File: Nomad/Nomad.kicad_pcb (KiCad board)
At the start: 2 copper layers, 61 parts, among them J1 Barrel_Jack, J2 Conn_01x04_Socket, J3 Conn_01x04_Socket, J4 Conn_01x02_Socket, J5 Conn_01x02_Socket, U1 ESP32-DEVKITC-32UE, U2 BU18SD5WG-TL, U3 BU33SD5WG-TR, U4 XL1509-5.0, U5 PTAS2780RYAR

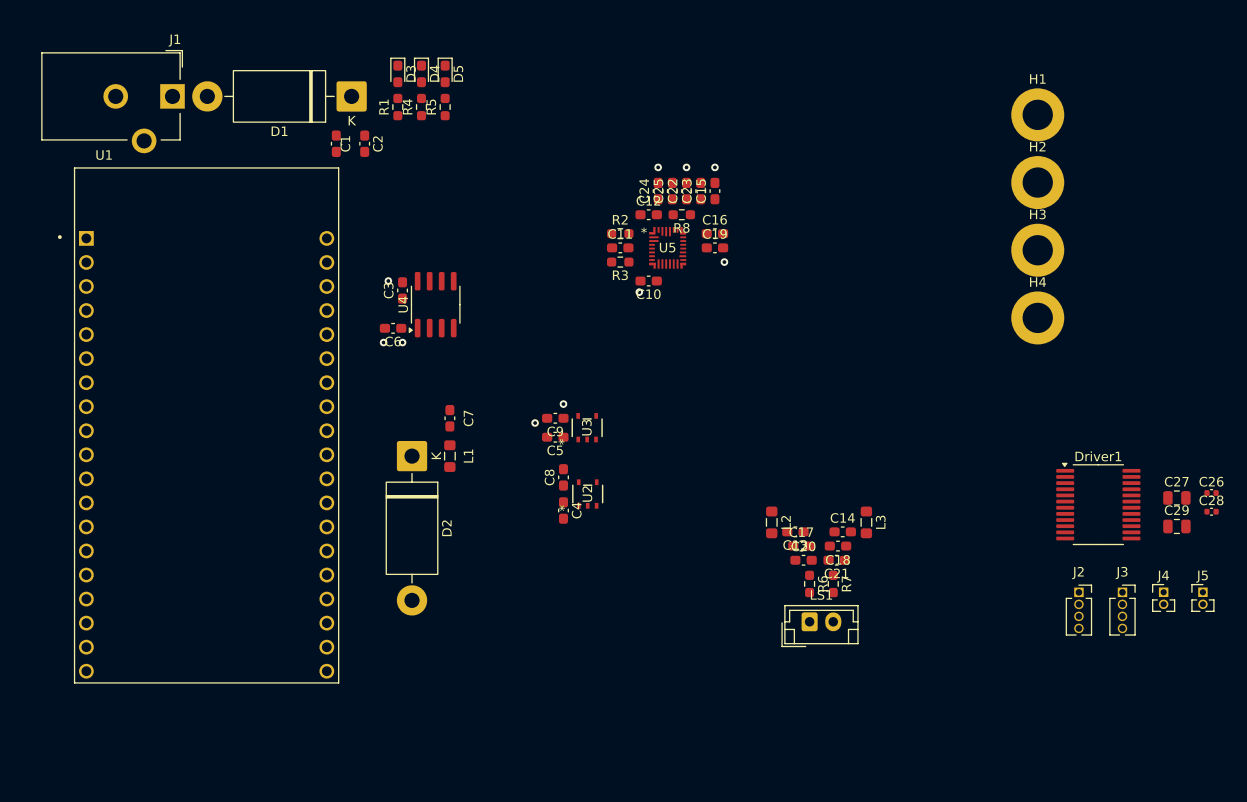
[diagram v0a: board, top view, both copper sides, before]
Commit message: routage pcb
finitions placement composants + routage
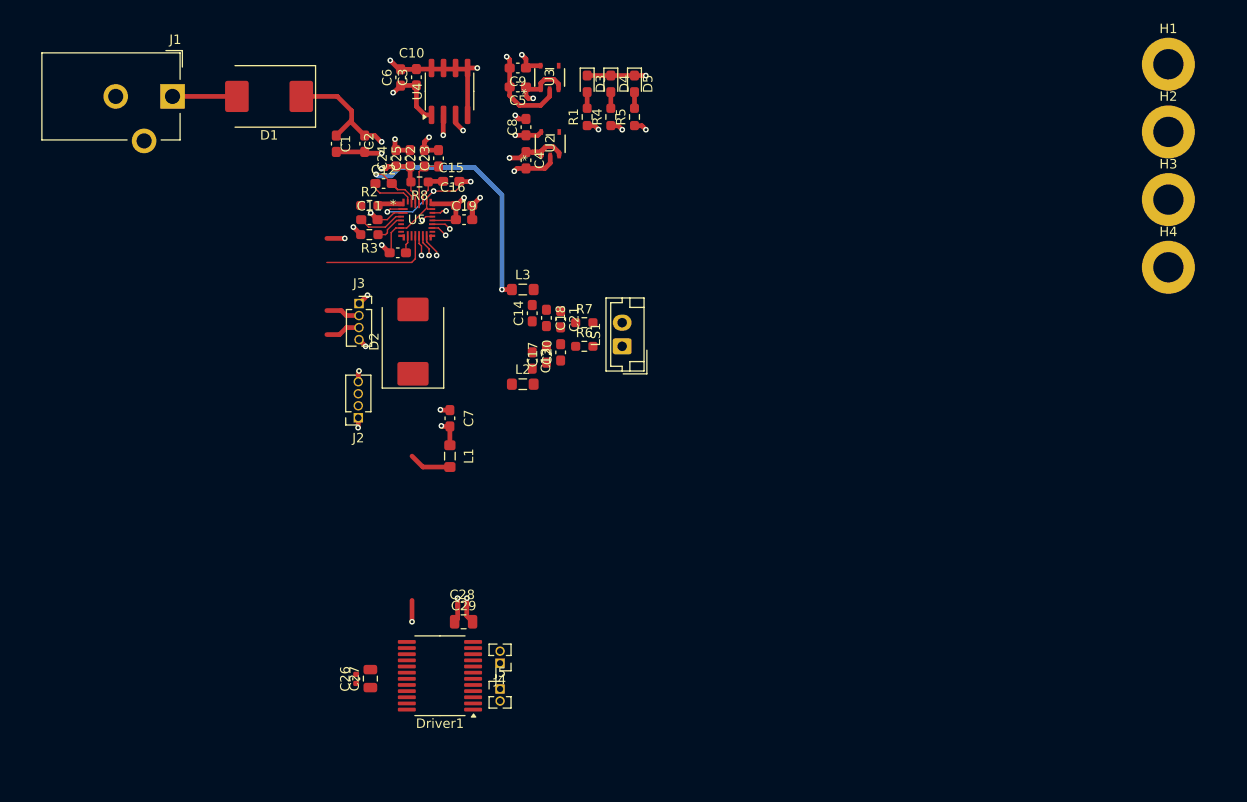
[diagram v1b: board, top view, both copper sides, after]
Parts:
- removed U1: ESP32-DEVKITC-32UE, footprints:ESPRESSIF_ESP32-DEVKITC-32UE
- D1, D2: value 1N5820 -> MBRS320; footprint Diode_THT:D_DO-201AD_P15.24mm_Horizontal -> Diode_SMD:D_SMC
- moved C26 92.5 mm to (108.1, 96.5), turned to 90 degrees
- moved C27 87.3 mm to (109.6, 96.5), turned to 90 degrees
- moved J3 86.2 mm to (108.4, 56.9)
- moved C28 79.8 mm to (119.3, 88.8)
- moved J2 78.3 mm to (108.3, 69.0), turned to 180 degrees
- moved C29 76.0 mm to (119.5, 90.5)
- moved J5 75.0 mm to (123.3, 97.6)
- moved Driver1 71.9 mm to (117.0, 96.2), turned to 180 degrees
- moved J4 70.5 mm to (123.3, 94.9), turned to 180 degrees
- moved L3 43.9 mm to (125.7, 55.4), turned to 0 degrees
- moved C14 40.1 mm to (126.7, 57.9), turned to 90 degrees
- moved C18 39.1 mm to (128.2, 58.4), turned to -90 degrees
- moved C21 38.7 mm to (129.7, 58.5), turned to -90 degrees
- moved R7 38.1 mm to (132.2, 58.9), turned to 0 degrees
- moved C4 37.2 mm to (126.0, 41.7)
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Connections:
- C26 pad 1: +3.3V -> 3.3V
- C27 pad 1: +3.3V -> 3.3V
- Driver1 pad 20: +3.3V -> 3.3V
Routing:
- net GND: track 0.00 -> 116.0 mm, vias 0 -> 20
- net 12V: track 0.00 -> 64.9 mm, vias 0 -> 5
- net /OUT_N: track 0.00 -> 32.4 mm, vias 0 -> 2
- net 5V: track 0.00 -> 31.4 mm, vias 0 -> 6
- net 1.8V: track 0.00 -> 26.7 mm, vias 0 -> 3
- net 3.3V: track 0.00 -> 18.5 mm, vias 0 -> 2
- net SDOUT: track 0.00 -> 11.9 mm
- net Net-(D1-A): track 0.00 -> 6.80 mm
- net Net-(D2-K): track 0.00 -> 6.64 mm, vias 0 -> 1
- net Net-(U5-VBAT1S): track 0.00 -> 5.64 mm
- net Net-(U5-BST_N): track 0.00 -> 5.56 mm
- net Net-(U5-BST_P): track 0.00 -> 4.99 mm
- net /OUT_P: track 0.00 -> 4.15 mm, vias 0 -> 1
- net Net-(U5-PVDD_SNS): track 0.00 -> 3.88 mm
- net Echo_cap_1: track 0.00 -> 3.71 mm
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- added copper zone on In2.Cu, net GND
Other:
- copper layers 2 -> 4

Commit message: Fin routage
Fin routage sauf pour esp
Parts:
- moved H1 96.6 mm to (109.1, 77.8)
- moved H2 86.2 mm to (107.9, 33.0)
- moved H4 63.2 mm to (136.0, 78.3)
- moved H3 62.8 mm to (135.4, 68.8)
- moved Driver1 48.7 mm to (131.0, 49.5)
- moved C28 48.7 mm to (133.3, 42.1)
- moved C29 48.7 mm to (133.5, 43.9)
- moved J4 48.7 mm to (137.3, 48.2)
- moved J5 48.7 mm to (137.3, 51.0)
- moved C26 48.7 mm to (122.2, 49.9)
- moved C27 48.7 mm to (123.7, 49.9)
- moved C7 35.6 mm to (122.1, 33.6)
- moved L1 35.6 mm to (122.1, 37.6)
- moved D2 6.90 mm to (119.5, 56.6), turned to -90 degrees
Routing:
- net GND: track 116.0 -> 142.6 mm, vias 20 -> 21
- net /OUT_P: track 4.15 -> 30.5 mm, vias 1 -> 2
- net 12V: track 64.9 -> 80.1 mm
- net Net-(D2-K): track 6.64 -> 21.7 mm, vias 1 -> 2
- net /VSNS_N: track 0.00 -> 12.9 mm
- net /VSNS_P: track 1.12 -> 13.9 mm
- net 3.3V: track 18.5 -> 25.0 mm, vias 2 -> 3
- net AO2: track 0.00 -> 3.68 mm
- net BO2: track 0.00 -> 3.65 mm
- net BO1: track 0.00 -> 3.63 mm
- net AO1: track 0.00 -> 3.61 mm
- net Net-(C20-Pad1): track 0.00 -> 2.21 mm
- net STBY: track 0.00 -> 2.16 mm, vias 0 -> 1
- net Net-(C21-Pad1): track 0.00 -> 2.09 mm

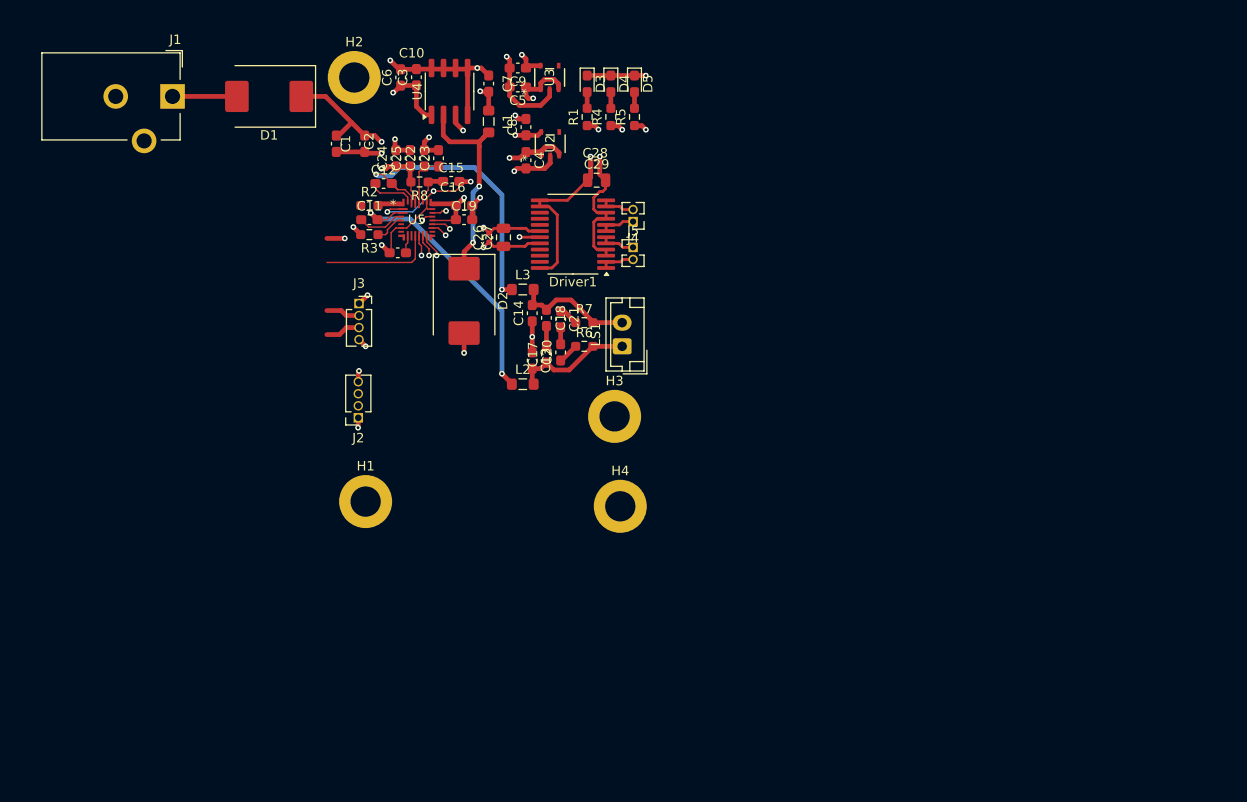
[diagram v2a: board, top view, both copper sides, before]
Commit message: Finished routing and silkscreen placement
todo Gerber
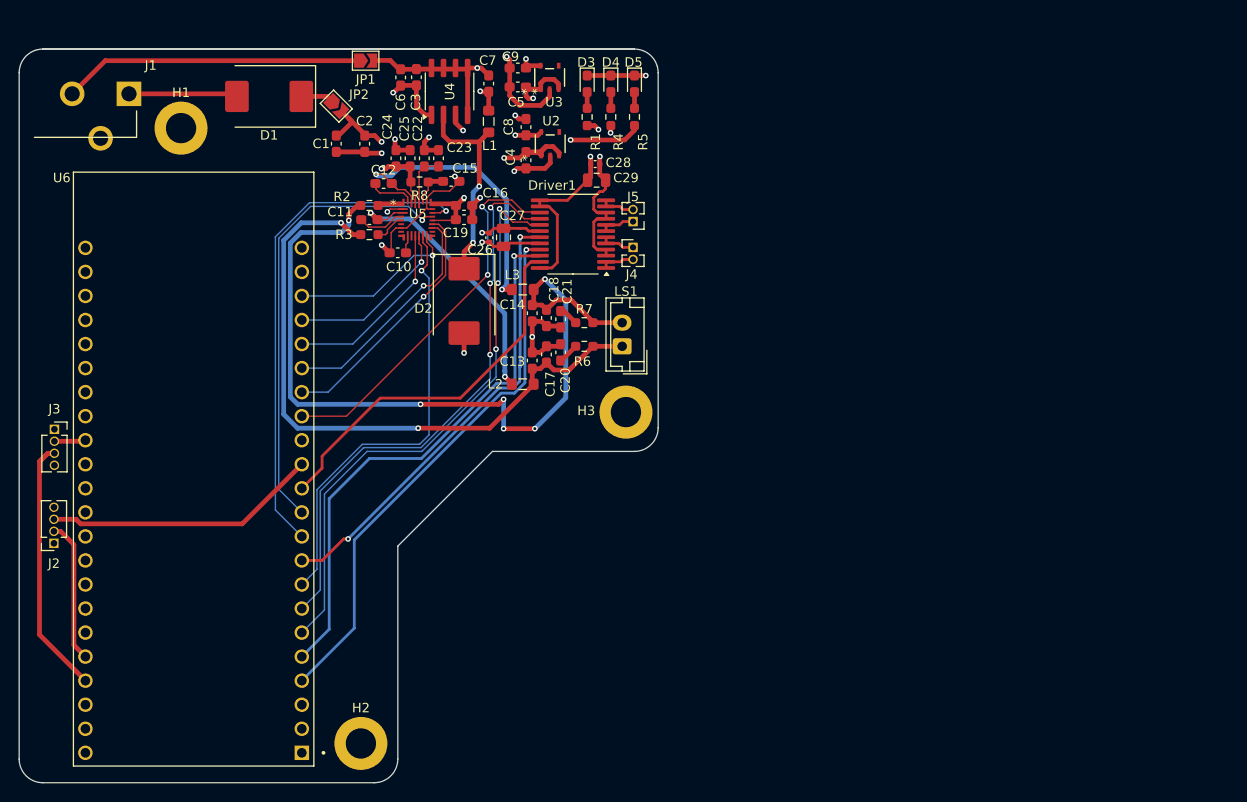
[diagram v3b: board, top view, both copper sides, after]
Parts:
- removed H4: MountingHole_Pad, MountingHole:MountingHole_3.2mm_M3_DIN965_Pad
- added JP1: SolderJumper_2_Open, Jumper:SolderJumper-2_P1.3mm_Open_TrianglePad1.0x1.5mm, F.Cu at (109.1, 31.2)
- added JP2: SolderJumper_2_Open, Jumper:SolderJumper-2_P1.3mm_Open_TrianglePad1.0x1.5mm, F.Cu at (106.0, 36.0)
- added U6: ESP32-S3-DEVKITC-1-N8R2, footprints:XCVR_ESP32-S3-DEVKITC-1-N8R2, F.Cu at (90.9, 74.4)
- moved H2 70.4 mm to (108.6, 103.3)
- moved H1 44.0 mm to (89.6, 38.4)
- moved J3 34.8 mm to (76.2, 70.2)
- moved J2 34.8 mm to (76.2, 82.2)
- moved J1 4.61 mm to (84.1, 34.7)
- moved H3 1.28 mm to (136.6, 68.3)
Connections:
- D1 pad 1: 12V -> Net-(D1-K)
- J1 pad 2: GND -> Net-(JP1-A)
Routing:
- net 3.3V: track 25.0 -> 105.9 mm
- net 5V: track 31.4 -> 109.9 mm, vias 6 -> 4
- net /VSNS_N: track 12.9 -> 88.1 mm, vias 0 -> 6
- net BIN1: track 0.00 -> 61.8 mm, vias 0 -> 3
- net BIN2: track 0.00 -> 60.5 mm, vias 0 -> 3
- net AIN2: track 0.00 -> 58.5 mm, vias 0 -> 1
- net AIN1: track 0.00 -> 57.6 mm, vias 0 -> 1
- net /VSNS_P: track 13.9 -> 69.6 mm, vias 1 -> 2
- net SDZ: track 1.53 -> 54.2 mm
- net IRQZ: track 1.22 -> 48.4 mm
- net STBY: track 2.16 -> 48.2 mm, vias 1 -> 2
- net FSYNC: track 2.35 -> 46.7 mm
- net PWMB: track 0.00 -> 40.2 mm, vias 0 -> 2
- net PWMA: track 0.00 -> 39.9 mm
- net GND: track 142.6 -> 105.6 mm, vias 21 -> 16
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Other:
- board outline added: 67.5 x 77.5 mm

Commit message: schéma ancien routage final ver
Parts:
- moved J5 32.2 mm to (136.2, 83.2)
- moved J4 32.2 mm to (136.2, 80.4)
- moved Driver1 32.2 mm to (130.2, 81.8)
- moved C28 32.2 mm to (132.1, 74.4)
- moved C29 32.2 mm to (132.2, 76.1)
- moved C26 31.9 mm to (121.0, 81.8)
- moved C27 31.9 mm to (122.5, 81.8)
- moved C17 10.9 mm to (128.8, 51.4)
- moved L2 10.9 mm to (126.2, 54.5)
- moved C18 10.9 mm to (128.8, 47.5)
- moved C20 10.9 mm to (130.2, 51.1)
- moved C21 10.9 mm to (130.2, 47.6)
- moved LS1 10.9 mm to (136.8, 50.5)
- moved R6 10.9 mm to (132.8, 50.5)
- moved R7 10.9 mm to (132.8, 48.0)
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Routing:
- net BIN1: track 61.8 -> 1.45 mm, vias 3 -> 0
- net BIN2: track 60.5 -> 1.62 mm, vias 3 -> 0
- net AIN1: track 57.6 -> 1.40 mm
- net AIN2: track 58.5 -> 2.74 mm, vias 1 -> 0
- net /VSNS_N: track 88.1 -> 37.3 mm, vias 6 -> 2
- net 12V: track 79.3 -> 36.4 mm, vias 5 -> 1
- net STBY: track 48.2 -> 7.88 mm, vias 2 -> 1
- net PWMB: track 40.2 -> 1.73 mm, vias 2 -> 0
- net PWMA: track 39.9 -> 1.91 mm
- net /VSNS_P: track 69.6 -> 41.6 mm
- net /OUT_N: track 32.8 -> 22.6 mm
- net /OUT_P: track 30.5 -> 22.6 mm
- net FSYNC: track 46.7 -> 43.0 mm
- net 3.3V: track 105.9 -> 103.8 mm
- net IRQZ: track 48.4 -> 46.9 mm
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- added copper zone on In1.Cu, net GND
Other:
- outline, holes or cut-outs redrawn
- board text added: "C-Laroche G-Vidon S-Remy A-Djokic A-Taillepierre J-Lepetit"
- board text added: "Nomad"

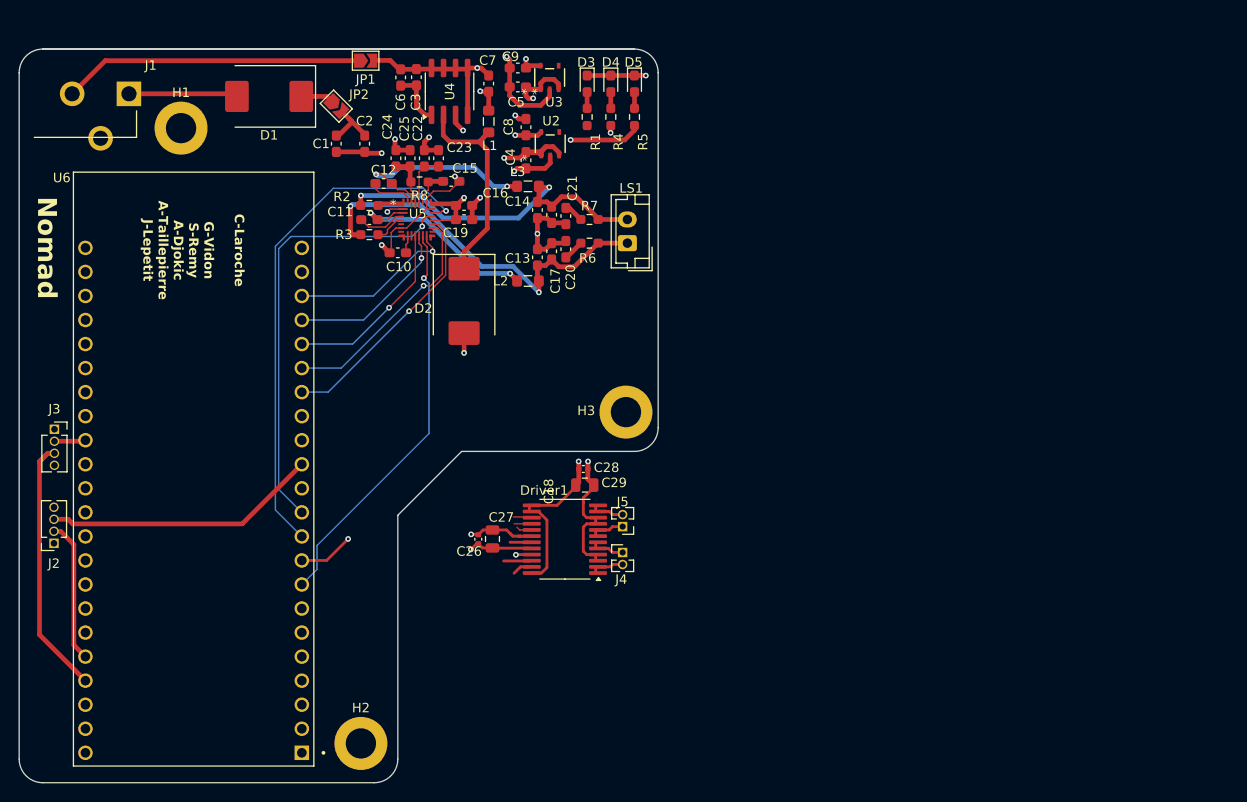
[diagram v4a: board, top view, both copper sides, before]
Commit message: encore plus de routage :(
Todo, rapprocher au max capa de découplage
grossir pistes alim au max
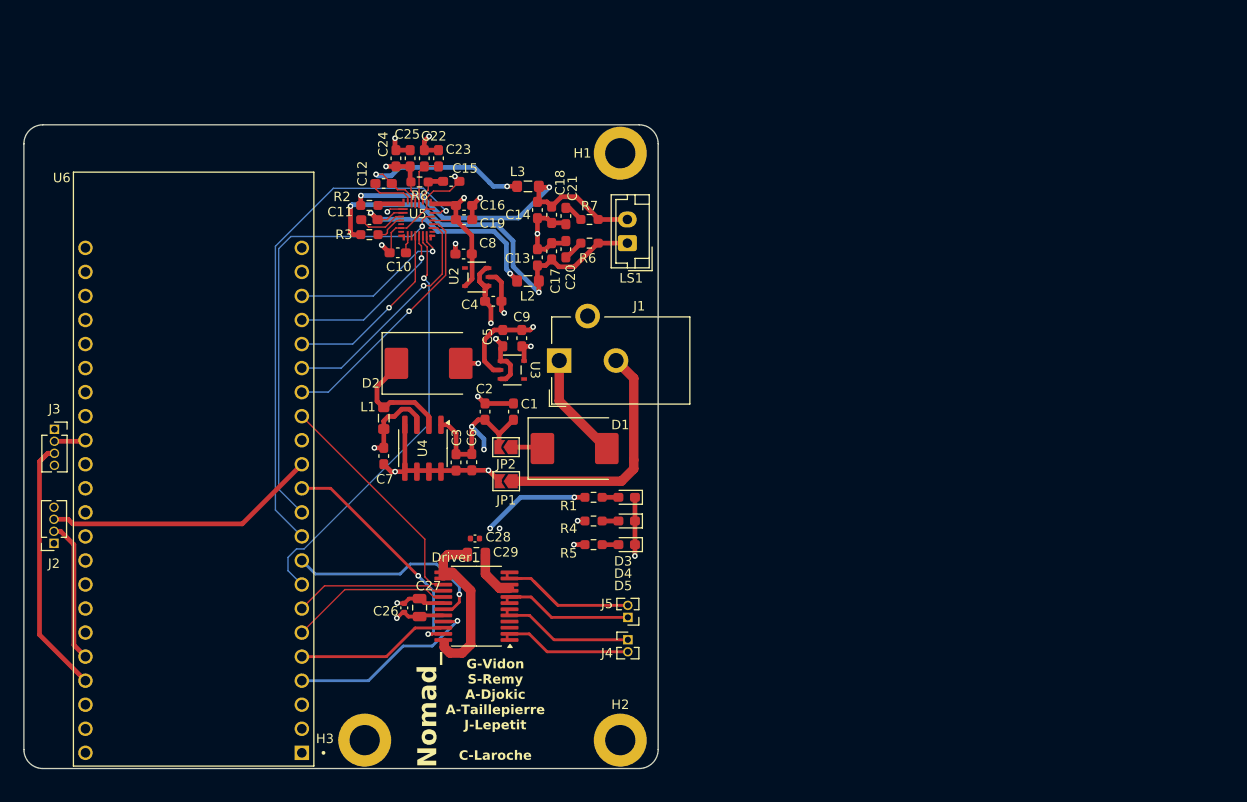
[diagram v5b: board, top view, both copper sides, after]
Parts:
- moved J1 53.5 mm to (129.6, 62.9), turned to 90 degrees
- moved D1 49.2 mm to (131.2, 72.2), turned to 0 degrees
- moved D5 48.7 mm to (136.7, 82.3), turned to 180 degrees
- moved JP1 46.8 mm to (124.0, 75.7), turned to 180 degrees
- moved H1 46.5 mm to (136.0, 41.0), turned to 180 degrees
- moved D4 46.2 mm to (136.7, 79.8), turned to 180 degrees
- moved R5 45.4 mm to (133.2, 82.3), turned to 0 degrees
- moved H3 44.3 mm to (109.0, 103.0)
- moved D3 43.9 mm to (136.7, 77.3), turned to 180 degrees
- moved R4 42.7 mm to (133.2, 79.8), turned to 0 degrees
- moved C6 41.3 mm to (120.3, 73.6), turned to -90 degrees
- moved C3 40.9 mm to (118.7, 73.7), turned to -90 degrees
- moved C7 40.9 mm to (111.0, 73.0), turned to -90 degrees
- moved JP2 40.2 mm to (123.9, 72.0), turned to 180 degrees
- moved R1 40.2 mm to (133.2, 77.3), turned to 0 degrees
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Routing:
- net 12V: track 36.4 -> 96.5 mm, vias 1 -> 5
- net 3.3V: track 103.8 -> 73.6 mm
- net 1.8V: track 34.7 -> 60.5 mm, vias 3 -> 2
- net PWMA: track 1.91 -> 24.8 mm, vias 0 -> 2
- net PWMB: track 1.73 -> 24.4 mm
- net AIN1: track 1.40 -> 20.6 mm
- net BO1: track 3.63 -> 19.3 mm
- net BIN1: track 1.45 -> 16.9 mm
- net STBY: track 7.88 -> 22.3 mm
- net BIN2: track 1.62 -> 15.9 mm
- net AIN2: track 2.74 -> 16.0 mm
- net BO2: track 3.65 -> 15.5 mm
- net Net-(D2-K): track 22.4 -> 10.9 mm
- net GND: track 104.6 -> 93.6 mm, vias 16 -> 17
- net AO2: track 3.68 -> 14.5 mm
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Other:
- board size 67.5 x 77.5 mm -> 67 x 68 mm
- board text added: "G-Vidon S-Remy A-Djokic A-Taillepierre J-Lepetit C-Laroche"
- board text added: "Nomad_"
- board text removed: "C-Laroche G-Vidon S-Remy A-Djokic A-Taillepierre J-Lepetit"
- board text removed: "Nomad"

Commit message: Fin routage
pls j'espère que c'est fini
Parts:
- moved H3 70.2 mm to (76.0, 41.0)
- moved C3 1.44 mm to (118.7, 72.2)
- moved C6 1.44 mm to (120.4, 72.2)
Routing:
- net GND: track 93.6 -> 120.8 mm
- net 1.8V: track 60.5 -> 53.5 mm
- net BO1: track 19.3 -> 14.3 mm
- net 3.3V: track 73.6 -> 75.6 mm
- net 5V: track 117.7 -> 116.4 mm, vias 3 -> 5
- net 12V: vias 5 -> 4

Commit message: fin routage
ok normalement là c'est bon
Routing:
- net GND: track 120.8 -> 125.3 mm
- net STBY: track 22.3 -> 21.4 mm
- net IRQZ: track 46.9 -> 46.4 mm
- net SDZ: track 54.9 -> 54.4 mm
